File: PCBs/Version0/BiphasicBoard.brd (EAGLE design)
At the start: 26.4 x 20 mm, 11 parts

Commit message: Editted design
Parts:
- removed R3, R4, R5: (no value), resistor:R0603
- removed U$2: (no value), TS3A4751:TS3A4751#2
- removed U$3: (no value), DS4432U+:DS4432U+
- added DS4432: (no value), DS4432U+:DS4432U+
- added R_PULLUP_RST, R_PULLUP_SCL, R_PULLUP_SDA: (no value), resistor:R0603
- added TS3A4751: (no value), TS3A4751:TS3A4751#2
- moved SV1 78.0 mm to (1.28, 9.44), turned to 270 degrees
- moved R2 71.2 mm to (17.9, 11.5)
- moved U$1 70.7 mm to (8.00, 10.5), turned to 270 degrees
- moved R1 69.4 mm to (14.9, 10.2), flipped to the top, turned to 90 degrees
- moved LOAD2 67.3 mm to (24.3, 11.6)
- moved LOAD1 56.3 mm to (24.4, 7.68)
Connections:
- net N$5 renamed TEST
- removed net N$12: LOAD1.1, U$2.2, U$2.3
- removed net N$13: LOAD2.1, U$2.10, U$2.9
- removed net N$3: R3.1, R4.2, R5.2, SV1.1, U$1.1, U$2.14, U$3.8
- removed net N$6: R5.1, SV1.4, U$1.16
- new net LOAD1: LOAD1.1, TS3A4751.2, TS3A4751.3
- new net LOAD2: LOAD2.1, TS3A4751.10, TS3A4751.9
- new net VDD: DS4432.8, R_PULLUP_RST.2, R_PULLUP_SCL.1, R_PULLUP_SDA.2, SV1.1, TS3A4751.14, U$1.1
- new net _RST: R_PULLUP_RST.1, SV1.4, U$1.16
- net CURRENT0: now also DS4432.6, TS3A4751.1, TS3A4751.8; no longer U$2.1, U$2.8, U$3.6
- net GND: now also DS4432.4, TS3A4751.11, TS3A4751.4, TS3A4751.7; no longer U$2.11, U$2.4, U$2.7, U$3.4
- net N$1: now also DS4432.2, R_PULLUP_SCL.2; no longer R3.2, U$3.2
- net N$10: now also TS3A4751.13; no longer U$2.13
- net N$11: now also TS3A4751.12; no longer U$2.12
- net N$2: now also DS4432.1, R_PULLUP_SDA.1; no longer R4.1, U$3.1
- net N$4: now also TS3A4751.5; no longer U$2.5
- net N$8: now also DS4432.5; no longer U$3.5
- net N$9: now also TS3A4751.6; no longer U$2.6
- net VIA1: now also DS4432.3; no longer U$3.3
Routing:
- net N$3: track 72.4 -> 0.00 mm
- net GND: track 62.3 -> 0.00 mm, vias 1 -> 5
- net VDD: track 0.00 -> 50.0 mm, vias 0 -> 1
- net _RST: track 0.00 -> 25.0 mm
- net LOAD2: track 0.00 -> 17.9 mm
- net N$10: track 24.4 -> 7.07 mm, vias 1 -> 0
- net TEST: track 5.87 -> 18.4 mm
- net N$4: track 10.3 -> 21.9 mm, vias 1 -> 2
- net N$11: track 17.5 -> 6.96 mm, vias 1 -> 0
- net LOAD1: track 0.00 -> 9.37 mm
- net N$2: track 12.8 -> 21.7 mm
- net N$13: track 8.32 -> 0.00 mm
- net N$9: track 13.2 -> 21.3 mm, vias 1 -> 2
- net N$6: track 7.65 -> 0.00 mm
- net CURRENT0: track 22.5 -> 28.4 mm, vias 1 -> 2
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- added copper zone on layer 1, net GND
- added copper zone on layer 16, net GND
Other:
- board size 26.4 x 20 mm -> 25.9 x 16.5 mm

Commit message: Updated Library Parts
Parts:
- removed DS4432: (no value), DS4432U+:DS4432U+
- removed R1, R2: (no value), resistor:R0603
- removed U$1: G2X[1/5]2---PW20, TI_MSP430_v16:PW20
- added DS4432U+: (no value), BiphasicBoard:8_PIN
- added MSP430: (no value), BiphasicBoard:20_PIN
- added R_INPUT_FS0, R_INPUT_FS1: (no value), BiphasicBoard:R0603
- LOAD1, LOAD2: device pinhead:1X01 -> BiphasicBoard:1X01
- R_PULLUP_RST, R_PULLUP_SCL, R_PULLUP_SDA: device resistor:R0603 -> BiphasicBoard:R0603
- SV1: device con-lstb:MA04-1 -> BiphasicBoard:MA04-1
- TS3A4751: device TS3A4751:TS3A4751#2 -> BiphasicBoard:14_PIN
- moved LOAD2 5.08 mm to (24.1, 6.55)
- moved LOAD1 4.45 mm to (24.2, 3.23)
- moved TS3A4751 2.32 mm to (16.3, 3.05), turned to 180 degrees
- moved R_PULLUP_SDA 0.64 mm to (4.83, 2.16)
- moved R_PULLUP_SCL 0.64 mm to (7.87, 1.65)
- moved R_PULLUP_RST 0.63 mm to (8.35, 14.8)
- moved SV1 0.63 mm to (1.28, 8.80)
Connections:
- removed net N$10: TS3A4751.13, U$1.11
- removed net N$11: TS3A4751.12, U$1.12
- new net IN1: MSP430.11, TS3A4751.13
- new net IN4: MSP430.12, TS3A4751.12
- net CURRENT0: now also DS4432U+.6; no longer DS4432.6
- net GND: now also DS4432U+.4, MSP430.20, R_INPUT_FS0.1, R_INPUT_FS1.1; no longer DS4432.4, R1.1, R2.1, U$1.20
- net N$1: now also DS4432U+.2, MSP430.14; no longer DS4432.2, U$1.14
- net N$2: now also DS4432U+.1, MSP430.15; no longer DS4432.1, U$1.15
- net N$4: now also MSP430.10; no longer U$1.10
- net N$8: now also DS4432U+.5, R_INPUT_FS0.2; no longer DS4432.5, R2.2
- net N$9: now also MSP430.9; no longer U$1.9
- net TEST: now also MSP430.17; no longer U$1.17
- net VDD: now also DS4432U+.8, MSP430.1; no longer DS4432.8, U$1.1
- net VIA1: now also DS4432U+.3, R_INPUT_FS1.2; no longer DS4432.3, R1.2
- net _RST: now also MSP430.16; no longer U$1.16
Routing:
- net N$10: track 7.07 -> 0.00 mm
- net N$11: track 6.96 -> 0.00 mm
- net IN1: track 0.00 -> 6.91 mm
- net IN4: track 0.00 -> 6.89 mm
- net LOAD2: track 17.9 -> 13.3 mm
- net LOAD1: track 9.37 -> 5.34 mm
- net N$4: track 21.9 -> 20.5 mm
- net N$9: track 21.3 -> 19.9 mm
- net CURRENT0: track 28.4 -> 29.2 mm
- net _RST: track 25.0 -> 25.6 mm

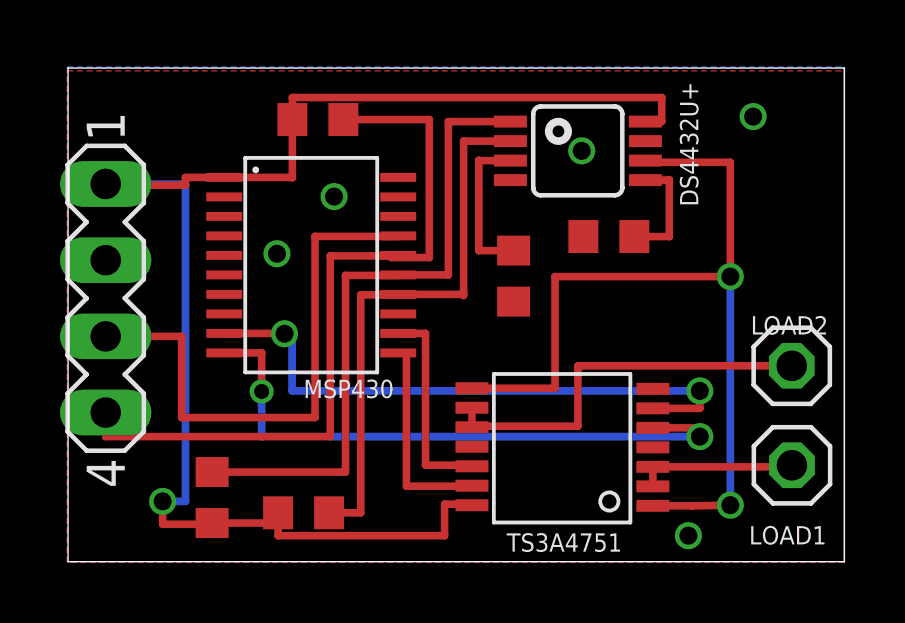
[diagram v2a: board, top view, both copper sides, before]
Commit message: Updated Board
Updated the board design to comply with the DRC of Seed_DRU
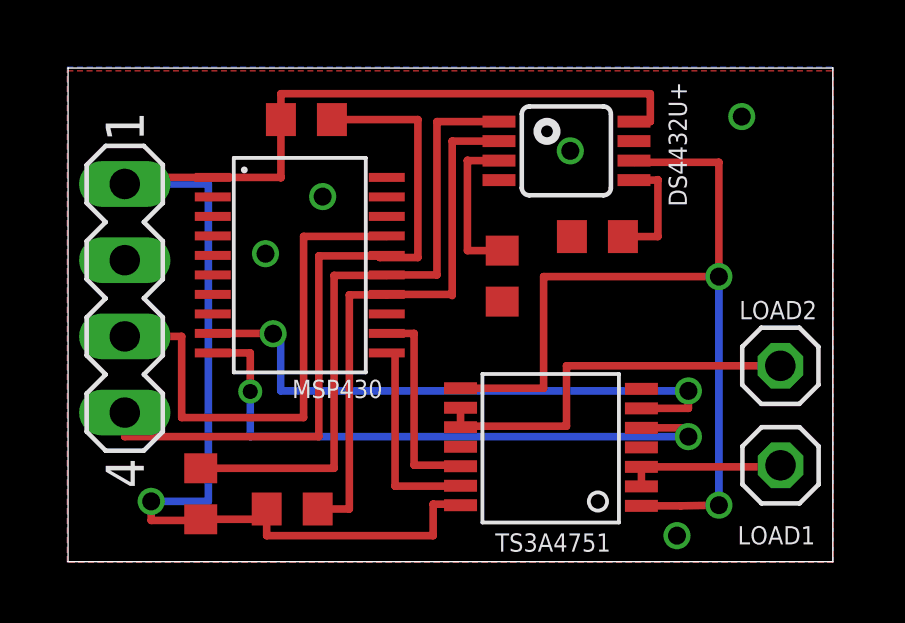
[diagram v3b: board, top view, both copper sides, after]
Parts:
- moved SV1 0.64 mm to (1.91, 8.80)
- moved R_PULLUP_SCL 0.40 mm to (7.49, 1.78)
- moved R_PULLUP_SDA 0.40 mm to (4.45, 2.29)
- moved DS4432U+ 0.38 mm to (16.6, 13.7)
- moved LOAD1 0.38 mm to (23.8, 3.23)
- moved LOAD2 0.38 mm to (23.8, 6.55)
- moved MSP430 0.38 mm to (7.75, 9.91)
- moved R_INPUT_FS0 0.38 mm to (17.7, 10.9)
- moved R_INPUT_FS1 0.38 mm to (14.5, 9.54)
- moved R_PULLUP_RST 0.38 mm to (7.97, 14.8)
- moved TS3A4751 0.38 mm to (15.9, 3.05)
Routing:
- net TEST: track 18.5 -> 17.5 mm
- net _RST: track 25.6 -> 24.6 mm
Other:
- board size 25.9 x 16.5 mm -> 25.5 x 16.5 mm
